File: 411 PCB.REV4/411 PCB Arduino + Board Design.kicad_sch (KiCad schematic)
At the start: 37 parts, among them J1 ICSP CONN, J3 Conn_01x04, J4 Conn_01x05_Pin, Q1 Q_NMOS_GDS, SW1 SW_SPST, SW2 SW_MEC_5E, SW3 SW_SPDT, SW4 SW_DPST_x2, U2 ATmega328P-P, Y1 8 MHz

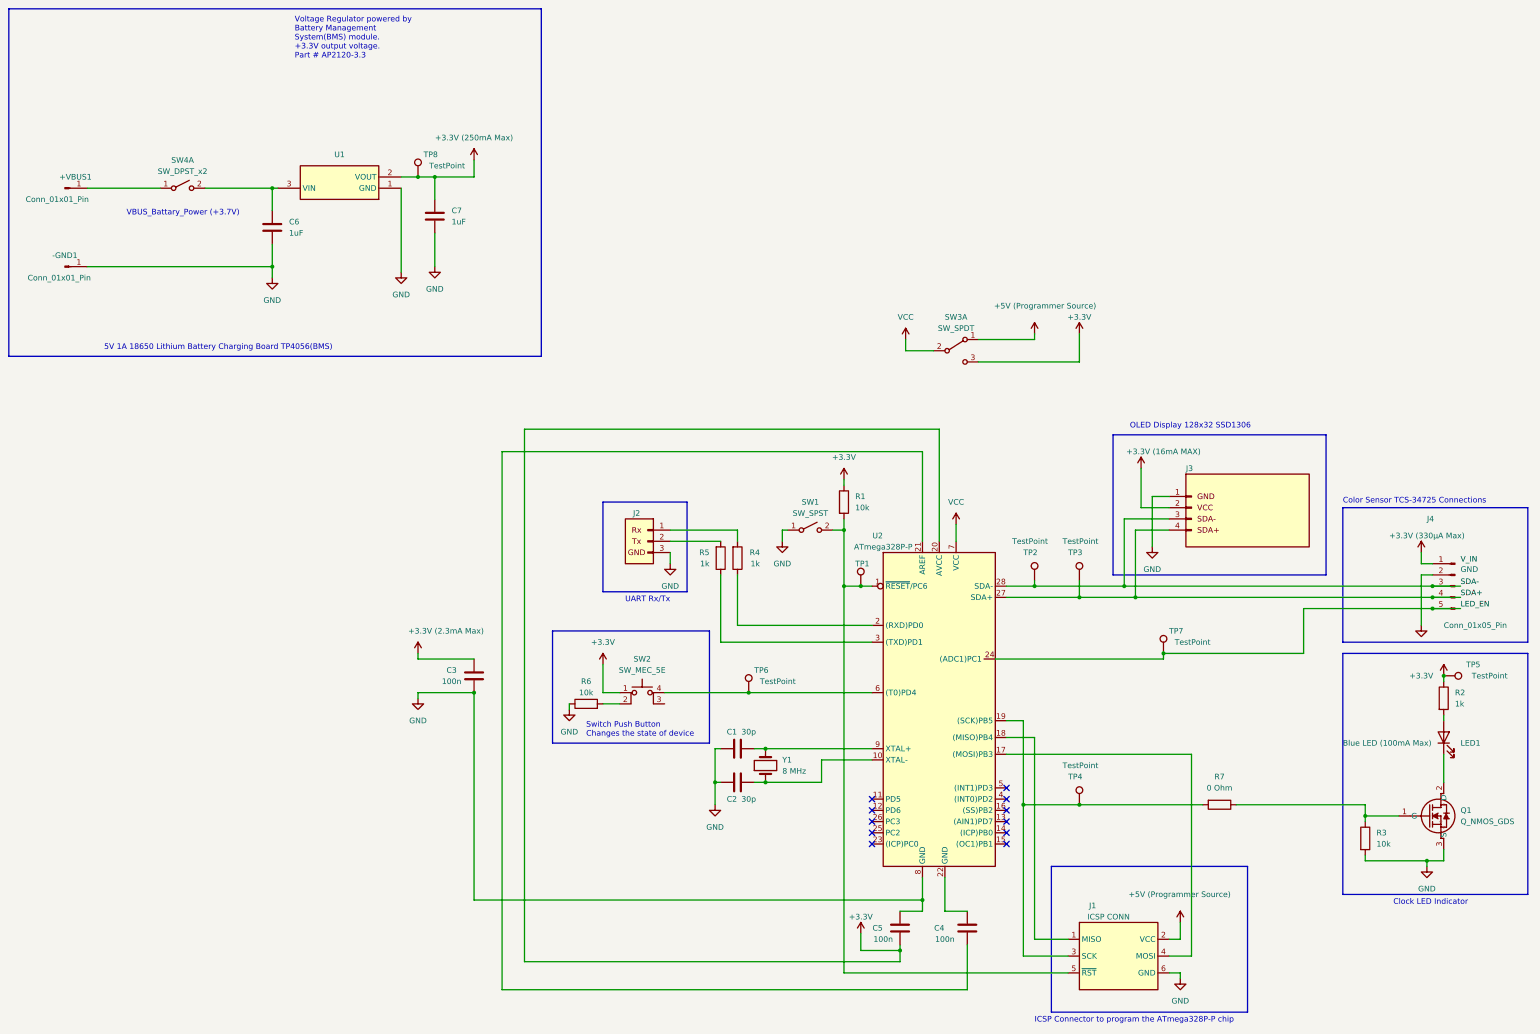
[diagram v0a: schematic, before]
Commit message: updated capacitators for crystal to 40pF
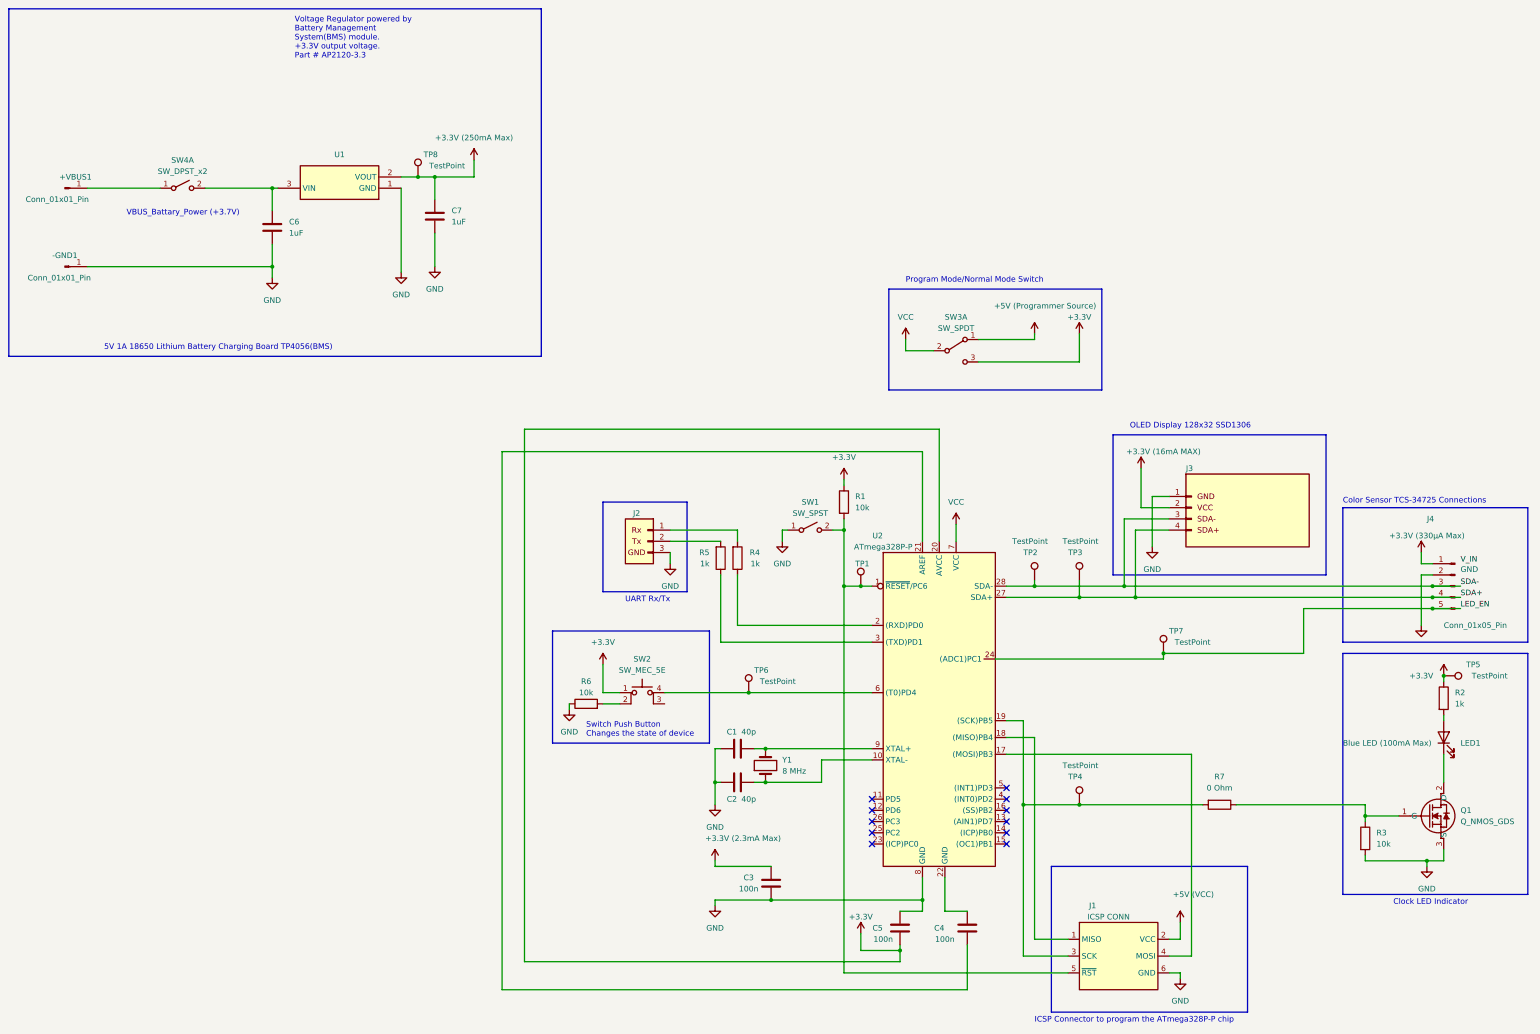
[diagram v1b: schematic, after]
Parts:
- C1, C2: value 30p -> 40p
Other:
- note added: "Program Mode/Normal Mode Switch"
- moved on the sheet: C3

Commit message: 43pF caps were the closest values of Digikey
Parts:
- C1, C2: value 40p -> 43p
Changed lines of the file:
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@@
       (effects (font (size 1.27 1.27)))
     )
-    (property "Value" "40p" (at 240.03 237.49 90)
+    (property "Value" "43p" (at 240.03 237.49 90)
       (effects (font (size 1.27 1.27)))
     )
@@
       (effects (font (size 1.27 1.27)))
     )
-    (property "Value" "40p" (at 240.03 222.25 90)
-      (effects (font (size 1.27 1.27)))
-    )
+    (property "Value" "43p" (at 240.03 222.25 90)
+      (effects (font (size 1.27 1.27)))
+    )
